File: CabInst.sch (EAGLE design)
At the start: 8 parts, among them J1 ZX62R-AB-5P, U1 FT231XS, U2 ESP-WROOM-32

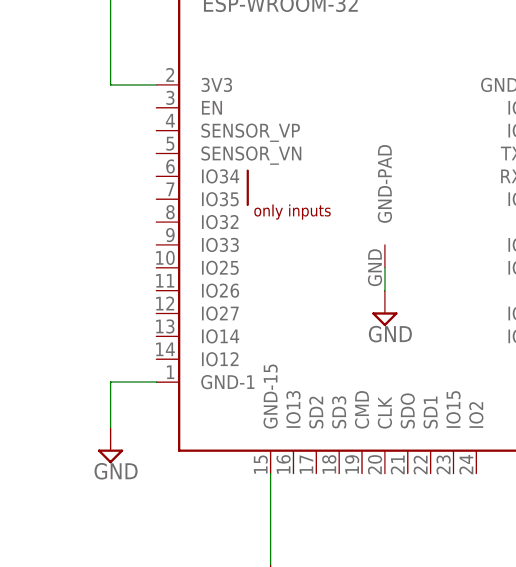
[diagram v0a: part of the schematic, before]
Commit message: [update] add esp32
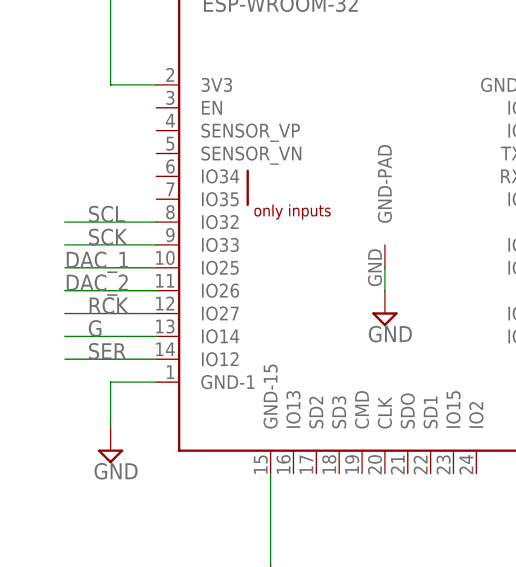
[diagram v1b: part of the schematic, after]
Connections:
- new net DAC_1: U2.IO25
- new net DAC_2: U2.IO26
- new net G: U2.IO14
- new net RCK: U2.IO27
- new net SCK: U2.IO33
- new net SCL: U2.IO32
- new net SER: U2.IO12
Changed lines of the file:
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@@
+</segment>
+</net>
+<net name="SER" class="0">
+<segment>
+<pinref part="U2" gate="G$1" pin="IO12"/>
+<wire x1="35.56" y1="60.96" x2="25.4" y2="60.96" width="0.1524" layer="91"/>
+<label x="27.94" y="60.96" size="1.778" layer="95"/>
+</segment>
+</net>
+<net name="G" class="0">
+<segment>
+<pinref part="U2" gate="G$1" pin="IO14"/>
+<wire x1="25.4" y1="63.5" x2="35.56" y2="63.5" width="0.1524" layer="91"/>
+<label x="27.94" y="63.5" size="1.778" layer="95"/>
+</segment>
+</net>
+<net name="RCK" class="0">
+<segment>
+<pinref part="U2" gate="G$1" pin="IO27"/>
+<wire x1="35.56" y1="66.04" x2="25.4" y2="66.04" width="0.1524" layer="91"/>
+<label x="27.94" y="66.04" size="1.778" layer="95"/>
+</segment>
+</net>
+<net name="SCK" class="0">
+<segment>
+<pinref part="U2" gate="G$1" pin="IO33"/>
+<wire x1="35.56" y1="73.66" x2="25.4" y2="73.66" width="0.1524" layer="91"/>
+<label x="27.94" y="73.66" size="1.778" layer="95"/>
+</segment>
+</net>
+<net name="SCL" class="0">
+<segment>
+<pinref part="U2" gate="G$1" pin="IO32"/>
+<wire x1="25.4" y1="76.2" x2="35.56" y2="76.2" width="0.1524" layer="91"/>
+<label x="27.94" y="76.2" size="1.778" layer="95"/>
+</segment>
+</net>
+<net name="DAC_2" class="0">
+<segment>
+<pinref part="U2" gate="G$1" pin="IO26"/>
+<wire x1="35.56" y1="68.58" x2="25.4" y2="68.58" width="0.1524" layer="91"/>
+<label x="25.4" y="68.58" size="1.778" layer="95"/>
+</segment>
+</net>
+<net name="DAC_1" class="0">
+<segment>
+<pinref part="U2" gate="G$1" pin="IO25"/>
+<wire x1="25.4" y1="71.12" x2="35.56" y2="71.12" width="0.1524" layer="91"/>
+<label x="25.4" y="71.12" size="1.778" layer="95"/>
 </segment>
 </net>

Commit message: [update]
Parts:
- added J2: 2DC-0415D200, CabInst:2DC-0415D200
- added LED1, LED2, LED3, LED4, LED5: (no value), CabInst:LEDCHIP-LED0603
- added Q1, Q2: MMSS8050-L, CabInst:MMSS8050-L
- added R10, R11, R12, R13, R14, R15, R16: (no value), CabInst:TRIM_EU-SM-42/43A
- added R3, R4: 10k, CabInst:R-EU_R0603
- added R5, R6, R7, R8, R9: (no value), CabInst:R-EU_R0603
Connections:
- new net +24V: J2.1
- new net EN: Q1.C, U2.EN
- new net IO0: Q2.E, U2.IO0
- new net LED1: R8.2
- new net LED2: R9.2
- new net N$10: LED5.A, R9.1
- new net N$12: LED4.A, R8.1
- new net N$5: LED1.A, R5.1
- new net N$6: LED2.A, R6.1
- new net N$7: Q2.B, R4.2
- new net N$8: Q1.B, R3.2
- new net N$9: LED3.A, R7.1
- net +3V3: now also R6.2, R7.2
- net +5V: now also R5.2
- net CBUS1: now also LED2.C
- net CBUS2: now also LED3.C
- net DTR: now also Q2.C, R3.1
- net GND: now also J2.2, J2.3, LED1.C, LED4.C, LED5.C
- net RTS: now also Q1.E, R4.1

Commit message: [update]
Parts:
- added R17: (no value), CabInst:TRIM_EU-SM-42/43A
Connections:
- new net N$11: R13.S
- new net N$13: R14.S
- new net N$14: R15.S
- new net N$15: R12.S
- new net N$16: R11.S
- new net N$17: R10.S
- new net N$18: R16.S
- new net N$19: R17.S
- new net N$21: U2.IO18
- new net N$22: U2.IO5
- new net N$23: U2.IO17
- new net N$24: U2.IO16
- new net N$25: U2.IO4
- new net N$27: U2.IO23
- new net N$28: U2.IO22
- new net N$31: U2.IO21
- new net N$33: U2.IO19
- new net PWM1: R10.E
- new net PWM2: R11.E
- new net PWM3: R12.E
- new net PWM4: R13.E
- new net PWM5: R14.E
- new net PWM6: R15.E
- new net PWM7: R16.E
- new net PWM8: R17.E
- net GND: now also R10.A, R11.A, R12.A, R13.A, R14.A, R15.A, R16.A, R17.A
- net RXD: now also U2.TXD0
- net TXD: now also U2.RXD0
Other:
- moved on the sheet: R10, R11, R12, R13, R14, R15, R16
